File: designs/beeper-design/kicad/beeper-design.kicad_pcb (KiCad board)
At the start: 4 copper layers, 27.5 x 19 mm, 100 parts

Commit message: kicad exported data
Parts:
- C1: footprint beeper-design:Pkg0603_2 -> beeper-design:Pkg0603
- C10: footprint beeper-design:Pkg0201_42 -> beeper-design:Pkg0201_37
- C11: value 10u -> 2.2u; footprint beeper-design:Pkg0402_8 -> beeper-design:Pkg0201_29
- C12: value 10u -> 2.2u; footprint beeper-design:Pkg0402 -> beeper-design:Pkg0201_48
- C13: value 1u -> 2.2u; footprint beeper-design:Pkg0201_10 -> beeper-design:Pkg0201_51
- C14: footprint beeper-design:Pkg0201_25 -> beeper-design:Pkg0201_18
- C15: value 470n -> 2.2u; footprint beeper-design:Pkg0201_21 -> beeper-design:Pkg0201_11
- C16: value 470n -> 2.2u; footprint beeper-design:Pkg0201_31 -> beeper-design:Pkg0201_27
- C17: value 22n -> 2.2u; footprint beeper-design:Pkg0201_45 -> beeper-design:Pkg0201_40
- C18: value 22n -> 2.2u; footprint beeper-design:Pkg0201_9 -> beeper-design:Pkg0201_53
- C19: value 10n -> 2.2u; footprint beeper-design:Pkg0201_18 -> beeper-design:Pkg0201_10
- C2: footprint beeper-design:Pkg0603 -> beeper-design:Pkg0603_1
- C20: value 10n -> 2.2u; footprint beeper-design:Pkg0201_30 -> beeper-design:Pkg0201_26
- C21: value 270p -> 2.2u; footprint beeper-design:Pkg0201_43 -> beeper-design:Pkg0201_39
- C22: value 10n -> 2.2u; footprint beeper-design:Pkg0201_7 -> beeper-design:Pkg0201_52
- C23: value 10u -> 2.2u; footprint beeper-design:Pkg0402_2 -> beeper-design:Pkg0201_9
- C24: value 4.7u -> 2.2u; footprint beeper-design:Pkg0402_6 -> beeper-design:Pkg0201_23
- C25: value 4.7u -> 2.2u; footprint beeper-design:Pkg0402_4 -> beeper-design:Pkg0201_16
- C26: value 1u -> 2.2u; footprint beeper-design:Pkg0201_27 -> beeper-design:Pkg0201_19
- C27: value 100n -> 2.2u; footprint beeper-design:Pkg0201_38 -> beeper-design:Pkg0201_33
- C28: value 1u -> 2.2u; footprint beeper-design:Pkg0201_5 -> beeper-design:Pkg0201_46
- C29: value 1u -> 2.2u; footprint beeper-design:Pkg0201_15 -> beeper-design:Pkg0201_3
- C3: footprint beeper-design:Pkg0603_1 -> beeper-design:Pkg0603_2
- C30: value 1u -> 2.2u; footprint beeper-design:Pkg0201_3 -> beeper-design:Pkg0201_43
- C31: value 1u -> 2.2u; footprint beeper-design:Pkg0201_13 -> beeper-design:Pkg0201
- C32: value 1u -> 2.2u; footprint beeper-design:Pkg0201_23 -> beeper-design:Pkg0201_12
- C36: value 100n -> 2.2u; footprint beeper-design:Pkg0201_8 -> beeper-design:Pkg0201_49
- C37: value 1u -> 2.2u; footprint beeper-design:Pkg0201_26 -> beeper-design:Pkg0201_17
- C38: value 1u -> 2.2u; footprint beeper-design:Pkg0201_37 -> beeper-design:Pkg0201_31
- C39: value 1u -> 2.2u; footprint beeper-design:Pkg0201_35 -> beeper-design:Pkg0201_28
- C42: value 100n -> 2.2u; footprint beeper-design:Pkg0201_29 -> beeper-design:Pkg0201_21
- C43: value 100n -> 2.2u; footprint beeper-design:Pkg0201_39 -> beeper-design:Pkg0201_34
- C47: value 1u -> 2.2u; footprint beeper-design:Pkg0201_40 -> beeper-design:Pkg0201_35
- C48: value 1u -> 2.2u; footprint beeper-design:Pkg0201_6 -> beeper-design:Pkg0201_47
- C49: value 1p -> 2.2u; footprint beeper-design:Pkg0201_16 -> beeper-design:Pkg0201_4
- C5: value 100n -> 2.2u; footprint beeper-design:Pkg0201_32 -> beeper-design:Pkg0201_24
- C50: value 1p -> 2.2u; footprint beeper-design:Pkg0201_33 -> beeper-design:Pkg0201_25
- C7: value 10u -> 2.2u; footprint beeper-design:Pkg0402_1 -> beeper-design:Pkg0201_50
- C8: value 10u -> 2.2u; footprint beeper-design:Pkg0402_3 -> beeper-design:Pkg0201_6
- C9: value 10u -> 2.2u; footprint beeper-design:Pkg0402_7 -> beeper-design:Pkg0201_22
- L1: footprint beeper-design:Pkg0201_14 -> beeper-design:Pkg0201_1
- L2: value 1u -> 470n; footprint beeper-design:Pkg0402_5 -> beeper-design:Pkg0201_14
- L3: value 1n -> 470n; footprint beeper-design:Pkg0201_24 -> beeper-design:Pkg0201_13
- L4: value 1n -> 470n; footprint beeper-design:Pkg0201_41 -> beeper-design:Pkg0201_36
- R1: footprint beeper-design:Pkg0201_4 -> beeper-design:Pkg0201_44
- R10: footprint beeper-design:Pkg0201_28 -> beeper-design:Pkg0201_20
- R12, R13: footprint beeper-design:Pkg0201_17 -> beeper-design:Pkg0201_5
- R14, R15: footprint beeper-design:Pkg0201_1 -> beeper-design:Pkg0201_42
- R16, R17: footprint beeper-design:Pkg0201_20 -> beeper-design:Pkg0201_8
- R18: footprint beeper-design:Pkg0201_44 -> beeper-design:Pkg0201_38
- R2: footprint beeper-design:Pkg0201_36 -> beeper-design:Pkg0201_32
- R3: value 196R -> 10K; footprint beeper-design:Pkg0201_2 -> beeper-design:Pkg0201_30
- R4: footprint beeper-design:Pkg0201_12 -> beeper-design:Pkg0201_2
- R5: footprint beeper-design:Pkg0201_22 -> beeper-design:Pkg0201_15
- R6: value 10K -> 196R; footprint beeper-design:Pkg0201_34 -> beeper-design:Pkg0201_45
- R7: footprint beeper-design:Pkg0201 -> beeper-design:Pkg0201_41
- R8: footprint beeper-design:Pkg0201_11 -> beeper-design:Pkg0201_54
- R9: footprint beeper-design:Pkg0201_19 -> beeper-design:Pkg0201_7
- moved ? 3.86 mm to (130.4, 115.8)
- moved ? 2.51 mm to (132.9, 115.8)
- moved ? 1.39 mm to (134.3, 115.8)
- moved R6 1.14 mm to (143.6, 100.8)
- moved R3 1.11 mm to (144.5, 101.4), turned to -90 degrees
- turned L2 to 90 degrees
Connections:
- net V14 renamed V14RF
- net VDDSYS renamed VDD1P8
- net VDD_A renamed VDD_IO
- net board-io_qsen-i3c_sda renamed mcu_q-i3c_sda
- net mcu_conn-uart_rx renamed mcu_mcu-uart_rx
- net mcu_mcu-dbg-m33_swdclk renamed mcu_dbg-m33_swdclk
- net mcu_mcu-dbg-m33_swdio renamed mcu_dbg-m33_swdio
- net rid_p1 renamed SHIELD
- R3 pad 1: FOD -> mcu_mcu-wpwr1_gpio
- R6 pad 1: mcu_mcu-wpwr1_gpio -> FOD
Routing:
- net GND: track 43.2 -> 48.7 mm, vias 85 -> 95
- net mcu_mcu-wpwr3_gpio: track 18.2 -> 14.2 mm
- net mcu_mcu-wpwr1_gpio: track 13.5 -> 15.0 mm
- net VBAT: track 6.40 -> 5.72 mm
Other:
- rule pad_to_mask_clearance: 0.051 -> 0

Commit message: another export
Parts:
- removed L3: 470n, beeper-design:Pkg0201_13
- removed L4: 470n, beeper-design:Pkg0201_36
- removed U13: ~, beeper-design:LP_6
- added R11: 0R, beeper-design:Pkg0201_53, F.Cu at (133.6, 115.9)
- added R19: 0R, beeper-design:Pkg0201_19, F.Cu at (131.4, 115.9)
- C10: footprint beeper-design:Pkg0201_37 -> beeper-design:Pkg0201_18
- C11: footprint beeper-design:Pkg0201_29 -> beeper-design:Pkg0201_13
- C12: footprint beeper-design:Pkg0201_48 -> beeper-design:Pkg0201_31
- C13: footprint beeper-design:Pkg0201_51 -> beeper-design:Pkg0201_34
- C14: footprint beeper-design:Pkg0201_18 -> beeper-design:Pkg0201_2
- C15: footprint beeper-design:Pkg0201_11 -> beeper-design:Pkg0201_51
- C16: footprint beeper-design:Pkg0201_27 -> beeper-design:Pkg0201_12
- C17: footprint beeper-design:Pkg0201_40 -> beeper-design:Pkg0201_25
- C18: footprint beeper-design:Pkg0201_53 -> beeper-design:Pkg0201_37
- C19: footprint beeper-design:Pkg0201_10 -> beeper-design:Pkg0201_49
- C20: footprint beeper-design:Pkg0201_26 -> beeper-design:Pkg0201_10
- C21: footprint beeper-design:Pkg0201_39 -> beeper-design:Pkg0201_23
- C22: footprint beeper-design:Pkg0201_52 -> beeper-design:Pkg0201_35
- C23: footprint beeper-design:Pkg0201_9 -> beeper-design:Pkg0201_48
- C24: footprint beeper-design:Pkg0201_23 -> beeper-design:Pkg0201_7
- C25: footprint beeper-design:Pkg0201_16 -> beeper-design:Pkg0201_22
- C26: footprint beeper-design:Pkg0201_19 -> beeper-design:Pkg0201_42
- C27: footprint beeper-design:Pkg0201_33 -> beeper-design:Pkg0201_4
- C28: footprint beeper-design:Pkg0201_46 -> beeper-design:Pkg0201_47
- C29: footprint beeper-design:Pkg0201_3 -> beeper-design:Pkg0201_30
- C30: footprint beeper-design:Pkg0201_43 -> beeper-design:Pkg0201_16
- C31: footprint beeper-design:Pkg0201 -> beeper-design:Pkg0201_29
- C32: footprint beeper-design:Pkg0201_12 -> beeper-design:Pkg0201_17
- C36: footprint beeper-design:Pkg0201_49 -> beeper-design:Pkg0201_33
- C37: footprint beeper-design:Pkg0201_17 -> beeper-design:Pkg0201_45
- C38: footprint beeper-design:Pkg0201_31 -> beeper-design:Pkg0201_3
- C39: footprint beeper-design:Pkg0201_28 -> beeper-design:Pkg0201_1
- C4: footprint beeper-design:Pkg0805 -> beeper-design:Pkg0805_1
- C42: footprint beeper-design:Pkg0201_21 -> beeper-design:Pkg0201_50
- C43: footprint beeper-design:Pkg0201_34 -> beeper-design:Pkg0201_9
- C47: footprint beeper-design:Pkg0201_35 -> beeper-design:Pkg0201_11
- C48: footprint beeper-design:Pkg0201_47 -> beeper-design:Pkg0201_24
- C49: footprint beeper-design:Pkg0201_4 -> beeper-design:Pkg0201_44
- C5: footprint beeper-design:Pkg0201_24 -> beeper-design:Pkg0201_6
- C50: footprint beeper-design:Pkg0201_25 -> beeper-design:Pkg0201_8
- C6: footprint beeper-design:Pkg0805_1 -> beeper-design:Pkg0805
- C7: footprint beeper-design:Pkg0201_50 -> beeper-design:Pkg0201_32
- C8: footprint beeper-design:Pkg0201_6 -> beeper-design:Pkg0201_46
- C9: footprint beeper-design:Pkg0201_22 -> beeper-design:Pkg0201_5
- L1: footprint beeper-design:Pkg0201_1 -> beeper-design:Pkg0201_40
- L2: footprint beeper-design:Pkg0201_14 -> beeper-design:Pkg0201_54
- R1: footprint beeper-design:Pkg0201_44 -> beeper-design:Pkg0201_27
- R10: footprint beeper-design:Pkg0201_20 -> beeper-design:Pkg0201_52
- R12, R13: footprint beeper-design:Pkg0201_5 -> beeper-design:Pkg0201_36
- R14, R15: footprint beeper-design:Pkg0201_42 -> beeper-design:Pkg0201_20
- R16, R17: footprint beeper-design:Pkg0201_8 -> beeper-design:Pkg0201_39
- R18: footprint beeper-design:Pkg0201_38 -> beeper-design:Pkg0201_21
- R2: footprint beeper-design:Pkg0201_32 -> beeper-design:Pkg0201_15
- R3: footprint beeper-design:Pkg0201_30 -> beeper-design:Pkg0201_14
- R4: footprint beeper-design:Pkg0201_2 -> beeper-design:Pkg0201_41
- R5: footprint beeper-design:Pkg0201_15 -> beeper-design:Pkg0201
- R6: footprint beeper-design:Pkg0201_45 -> beeper-design:Pkg0201_28
- R7: footprint beeper-design:Pkg0201_41 -> beeper-design:Pkg0201_26
- R8: footprint beeper-design:Pkg0201_54 -> beeper-design:Pkg0201_38
- R9: footprint beeper-design:Pkg0201_7 -> beeper-design:Pkg0201_43
- U12: footprint beeper-design:LP_8 -> beeper-design:LP_7
- U3: footprint beeper-design:LP_7 -> beeper-design:LP_6
- moved TP1 6.63 mm to (131.7, 99.5)
- moved TP2 5.61 mm to (132.8, 99.5)
- moved TP12 5.60 mm to (143.0, 99.5)
- moved TP11 5.49 mm to (141.7, 99.6)
- moved ? 5.35 mm to (135.7, 115.5)
- moved ? 3.77 mm to (130.5, 115.7)
- moved ? 3.01 mm to (134.3, 115.9)
- moved C25 2.65 mm to (137.0, 102.2)
- moved U7 2.26 mm to (137.3, 103.3), turned to 0 degrees
- moved TP3 2.16 mm to (152.2, 109.1)
- moved TP13 2.15 mm to (150.7, 99.5)
- moved C11 1.76 mm to (141.0, 107.9)
- moved TP4 1.56 mm to (152.3, 107.9)
- moved ? 1.51 mm to (137.2, 115.1)
- moved TP14 1.21 mm to (149.4, 99.5)
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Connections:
- net mcu_dbg-m33_swdio renamed mcu_mcu-dbg-m33_swdio
- net mcu_mcu-uart_rx renamed mcu_conn-uart_rx
- net mcu_mcu-uart_tx renamed mcu_conn-uart_tx
- net mcu_q-i3c_sda renamed board-io_qsen-i3c_sda
- C11 pad 2: VDD1P8 -> VDDSYS
- C12 pad 2: VDD1P8 -> VDDSYS
- C13 pad 2: VDD1P8 -> V18F
- C14 pad 2: VDD1P8 -> VBUS
- C26 pad 2: VDD_IO -> VDD3P0
- C28 pad 2: VDD_IO -> VDD1P8P
- C29 pad 2: VDD1P8 -> VDDSYS
- C32 pad 2: VDD_IO -> VDD3P0
- C48 pad 2: VDD1P8 -> VDDSYS
- C6 pad 2: V18P -> VDD1P8P
- C9 pad 2: mcu_VBUS -> VBUS
- J1 pad 1: VDD1P8 -> VBUS
- L2 pad 2: VDD1P8 -> VDDSYS
- R1 pad 2: V18P -> VDD1P8P
- R12 pad 2: VDD1P8 -> VDD1P8P
- R13 pad 2: VDD1P8 -> VDD1P8P
- R16 pad 2: VDD1P8 -> VDDSYS
- R17 pad 2: VDD1P8 -> VDDSYS
- U1 pad J2: V18P -> VDD1P8P
- U1 pad M3: VDD1P8 -> VDDSYS
- U1 pad M5: mcu_VBUS -> VBUS
- U12 pad C2: VDD1P8 -> VDDSYS
- U2 pad B2: VDD1P8 -> V18F
- U3 pad D1: VDD1P8 -> VBUS
- U3 pad D2: VDD1P8 -> VBUS
- U3 pad D3: VDD1P8 -> VBUS
- U3 pad D4: VDD1P8 -> VBUS
- U3 pad F3: nAD-EN -> (no net)
- U4 pad A11: VDD1P8 -> VDDSYS
- U4 pad B14: VDD_IO -> VDD3P0
- U4 pad B6: VDD_IO -> VDD1P8P
- U4 pad D10: VDD_IO -> VDD3P0
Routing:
- net VBUS: track 10.9 -> 52.0 mm, vias 1 -> 2
- net VDD3P0: track 1.77 -> 28.2 mm, vias 0 -> 5
- net VDD1P8P: track 0.00 -> 22.8 mm, vias 0 -> 4
- net VDD_IO: track 11.3 -> 0.00 mm, vias 2 -> 0
- net nAD-EN: track 10.9 -> 0.00 mm, vias 3 -> 0
- net VDDSYS: track 0.00 -> 6.88 mm, vias 0 -> 7
- net VDD1P8: track 29.8 -> 23.1 mm, vias 19 -> 6
- net OUT+: track 1.64 -> 8.04 mm
- net VBAT: track 5.72 -> 10.4 mm
- net OUT-: track 1.47 -> 5.81 mm
- net V18P: track 3.88 -> 0.00 mm
- net mcu_VBUS: track 3.42 -> 0.00 mm
- net SHIELD: track 10.2 -> 7.91 mm, vias 2 -> 1
- net D-: track 20.3 -> 18.3 mm
- net cap_p1: track 1.42 -> 3.30 mm
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- added copper zone on In2.Cu, net VDDSYS
- removed copper zone on In2.Cu, net VDD1P8
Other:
- rule pad_to_mask_clearance: 0 -> 0.051

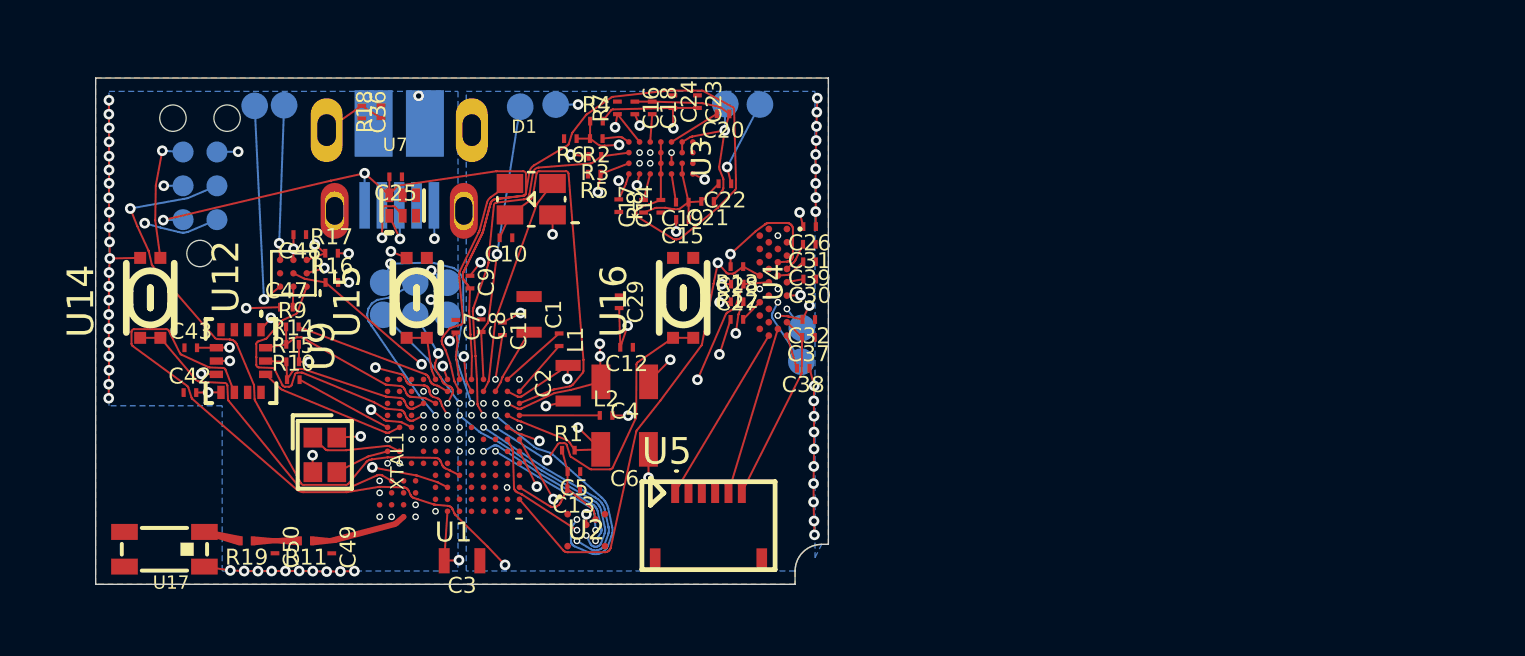
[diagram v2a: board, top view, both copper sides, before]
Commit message: crash with new usb connector
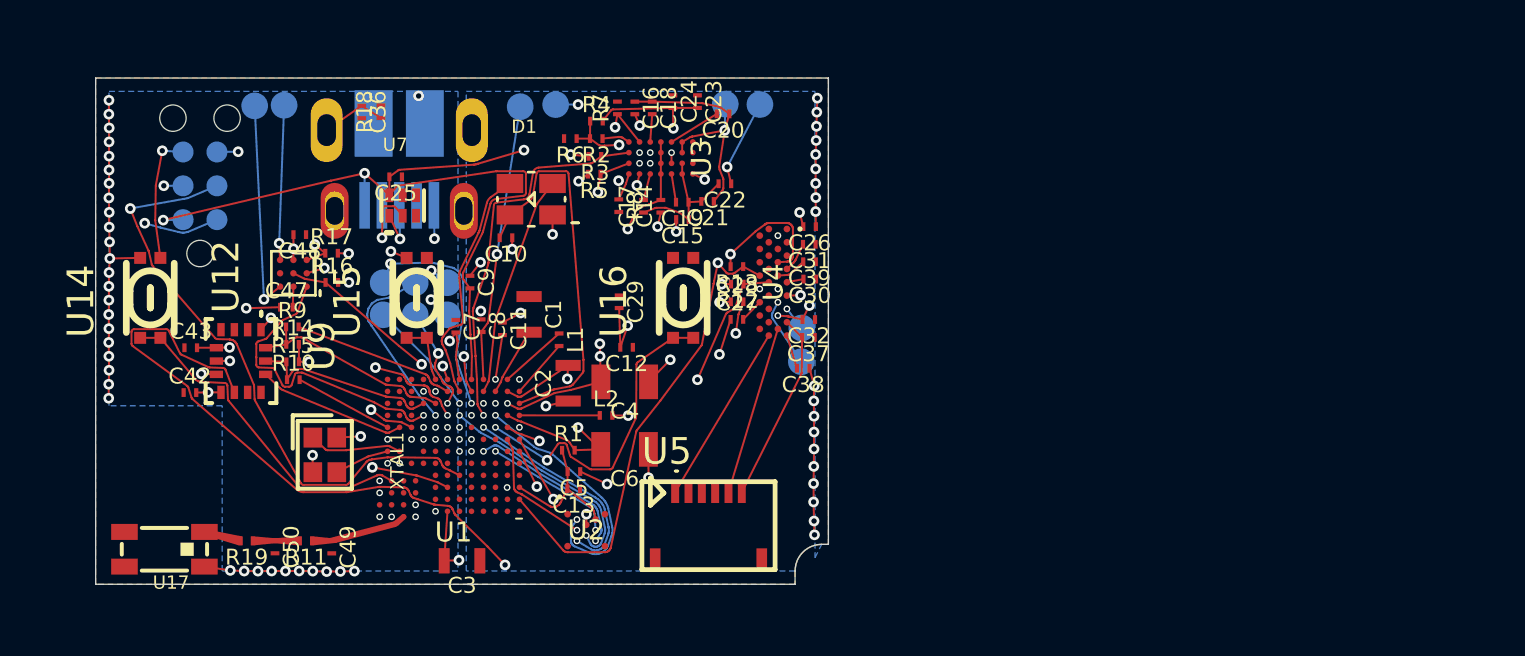
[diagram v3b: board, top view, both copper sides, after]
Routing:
- net VBUS: track 52.0 -> 40.2 mm, vias 2 -> 4
- net GND: track 48.6 -> 51.2 mm, vias 96 -> 100
- net (no net): track 1.02 -> 0.00 mm, vias 2 -> 0
- net 0: track 0.00 -> 1.02 mm, vias 0 -> 2
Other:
- net class BGA added: clearance 0.065, trace_width 0.075, via_dia 0.015, via_drill 0.15
- net class Default added: clearance 0.0625, trace_width 0.075, via_dia 0.015, via_drill 0.15
- net class RF added: clearance 0.0625, trace_width 0.221435, via_dia 0.015, via_drill 0.15

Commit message: new export
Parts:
- C10: footprint beeper-design:Pkg0201_18 -> beeper-design:Pkg0201_12
- C11: footprint beeper-design:Pkg0201_13 -> beeper-design:Pkg0201_5
- C12: footprint beeper-design:Pkg0201_31 -> beeper-design:Pkg0201_25
- C13: footprint beeper-design:Pkg0201_34 -> beeper-design:Pkg0201_28
- C14: footprint beeper-design:Pkg0201_2 -> beeper-design:Pkg0201
- C15: footprint beeper-design:Pkg0201_51 -> beeper-design:Pkg0201_50
- C16: footprint beeper-design:Pkg0201_12 -> beeper-design:Pkg0201_9
- C17: footprint beeper-design:Pkg0201_25 -> beeper-design:Pkg0201_22
- C18: footprint beeper-design:Pkg0201_37 -> beeper-design:Pkg0201_36
- C20: footprint beeper-design:Pkg0201_10 -> beeper-design:Pkg0201_7
- C21: footprint beeper-design:Pkg0201_23 -> beeper-design:Pkg0201_20
- C22: footprint beeper-design:Pkg0201_35 -> beeper-design:Pkg0201_33
- C24: footprint beeper-design:Pkg0201_7 -> beeper-design:Pkg0201_6
- C25: footprint beeper-design:Pkg0201_22 -> beeper-design:Pkg0201_18
- C26: footprint beeper-design:Pkg0201_42 -> beeper-design:Pkg0201_34
- C27: footprint beeper-design:Pkg0201_4 -> beeper-design:Pkg0201_53
- C28: footprint beeper-design:Pkg0201_47 -> beeper-design:Pkg0201_42
- C29: footprint beeper-design:Pkg0201_30 -> beeper-design:Pkg0201_24
- C30: footprint beeper-design:Pkg0201_16 -> beeper-design:Pkg0201_8
- C31: footprint beeper-design:Pkg0201_29 -> beeper-design:Pkg0201_21
- C32: footprint beeper-design:Pkg0201_17 -> beeper-design:Pkg0201_11
- C36: footprint beeper-design:Pkg0201_33 -> beeper-design:Pkg0201_30
- C37: footprint beeper-design:Pkg0201_45 -> beeper-design:Pkg0201_39
- C38: footprint beeper-design:Pkg0201_3 -> beeper-design:Pkg0201_51
- C39: footprint beeper-design:Pkg0201_1 -> beeper-design:Pkg0201_47
- C42: footprint beeper-design:Pkg0201_50 -> beeper-design:Pkg0201_43
- C43: footprint beeper-design:Pkg0201_9 -> beeper-design:Pkg0201_3
- C47: footprint beeper-design:Pkg0201_11 -> beeper-design:Pkg0201_4
- C48: footprint beeper-design:Pkg0201_24 -> beeper-design:Pkg0201_16
- C49: footprint beeper-design:Pkg0201_44 -> beeper-design:Pkg0201_37
- C5: footprint beeper-design:Pkg0201_6 -> beeper-design:Pkg0201_1
- C50: footprint beeper-design:Pkg0201_8 -> beeper-design:Pkg0201_2
- C7: footprint beeper-design:Pkg0201_32 -> beeper-design:Pkg0201_26
- C8: footprint beeper-design:Pkg0201_46 -> beeper-design:Pkg0201_41
- C9: footprint beeper-design:Pkg0201_5 -> beeper-design:Pkg0201_54
- J6: footprint beeper-design:AMPHENOL_10103594_0001LF -> beeper-design:GCT_USB3100_XX_X_REVB_1
- L1: footprint beeper-design:Pkg0201_40 -> beeper-design:Pkg0201_32
- L2: footprint beeper-design:Pkg0201_54 -> beeper-design:Pkg0201_46
- R1: footprint beeper-design:Pkg0201_27 -> beeper-design:Pkg0201_19
- R10: footprint beeper-design:Pkg0201_52 -> beeper-design:Pkg0201_44
- R11: footprint beeper-design:Pkg0201_53 -> beeper-design:Pkg0201_45
- R12, R13: footprint beeper-design:Pkg0201_36 -> beeper-design:Pkg0201_29
- R14, R15: footprint beeper-design:Pkg0201_20 -> beeper-design:Pkg0201_14
- R16, R17: footprint beeper-design:Pkg0201_39 -> beeper-design:Pkg0201_31
- R18: footprint beeper-design:Pkg0201_21 -> beeper-design:Pkg0201_17
- R19: footprint beeper-design:Pkg0201_19 -> beeper-design:Pkg0201_13
- R3: footprint beeper-design:Pkg0201_14 -> beeper-design:Pkg0201_10
- R4: footprint beeper-design:Pkg0201_41 -> beeper-design:Pkg0201_40
- R5: footprint beeper-design:Pkg0201 -> beeper-design:Pkg0201_52
- R6: footprint beeper-design:Pkg0201_28 -> beeper-design:Pkg0201_27
- R7: footprint beeper-design:Pkg0201_26 -> beeper-design:Pkg0201_23
- R9: footprint beeper-design:Pkg0201_43 -> beeper-design:Pkg0201_35
- moved TP1 8.22 mm to (127.1, 106.3)
- moved TP2 8.06 mm to (127.1, 105.2)
- moved C26 3.22 mm to (152.6, 107.3)
- moved C21 1.99 mm to (149.4, 101.3)
- moved TP11 1.34 mm to (143.0, 99.5)
- moved TP12 1.15 mm to (144.2, 99.5)
- moved R13 0.91 mm to (149.8, 104.7), turned to 90 degrees
- moved C25 0.87 mm to (137.2, 101.4), turned to 0 degrees
- moved R12 0.87 mm to (149.8, 105.4), turned to 90 degrees
- moved U7 0.84 mm to (137.7, 102.5)
- moved C28 0.80 mm to (149.8, 106.1)
- moved J6 0.49 mm to (137.1, 100.0)
- moved C37 0.46 mm to (152.5, 108.7)
- moved C32 0.44 mm to (152.6, 108.0)
- turned R18 to 0 degrees
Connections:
- net V14RF renamed V14
- net mcu_conn-uart_tx renamed mcu_mcu-uart_tx
- net mcu_dbg-m33_swdclk renamed mcu_mcu-dbg-m33_swdclk
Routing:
- net QVAR2: track 23.1 -> 6.47 mm, vias 1 -> 2
- net mcu_mcu-etm_data2: track 13.3 -> 7.71 mm
- net VBUS: track 40.2 -> 35.9 mm
- net SHIELD: track 7.91 -> 11.6 mm
- net VDD1P8P: track 22.8 -> 19.2 mm, vias 4 -> 1
- net VDD3P0: track 28.2 -> 25.1 mm, vias 5 -> 3
- net GND: track 51.2 -> 53.7 mm, vias 100 -> 101
- net codec-i2c-net_scl: track 18.0 -> 15.6 mm, vias 1 -> 3
- net OUT+: track 8.04 -> 5.77 mm
- net AC2: track 10.2 -> 8.80 mm
- net AC1: track 5.38 -> 6.53 mm
- net D-: track 18.3 -> 17.6 mm
- net codec-i2c-net_sda: track 12.7 -> 13.4 mm, vias 2 -> 3
- net VBAT: track 10.4 -> 10.9 mm
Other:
- outline, holes or cut-outs redrawn

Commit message: reasonble export
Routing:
- net QVAR2: track 6.47 -> 13.0 mm
- net mcu_mcu-etm_clk: track 8.50 -> 6.83 mm
- net VDD1P8: track 23.1 -> 21.5 mm, vias 6 -> 4
- net VBUS: track 35.9 -> 34.5 mm
- net 0: track 1.02 -> 0.00 mm, vias 2 -> 0
- net VDD1P8P: track 19.2 -> 18.3 mm, vias 1 -> 0
- net mcu_mcu-etm_data2: vias 3 -> 2
- net mcu_mcu-wpwr1_gpio: vias 1 -> 0
- net mcu_hap-gpio0_gpio: vias 1 -> 0
- net mcu_mcu-mem_sdio1: vias 1 -> 0
- net mcu_mcu-etm_data1: vias 2 -> 1

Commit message: cleaned up kicad export files
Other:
- net class BGA removed
- net class Default removed
- net class RF removed
- rule pad_to_mask_clearance: 0.051 -> 0
